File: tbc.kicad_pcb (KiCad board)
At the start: 2 copper layers, 161.3 x 77.6 mm, 51 parts, among them J1 5749181-1, J2 PJRAN1X1U01X, J3 PJRAN1X1U01X, J4 5749181-1, J5 PJRAN1X1U01X, J6 PJRAN3X1U03X, J7 4840.2201, Q1 BSS308PE, SW2 A11AH, U1 SAA7114H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

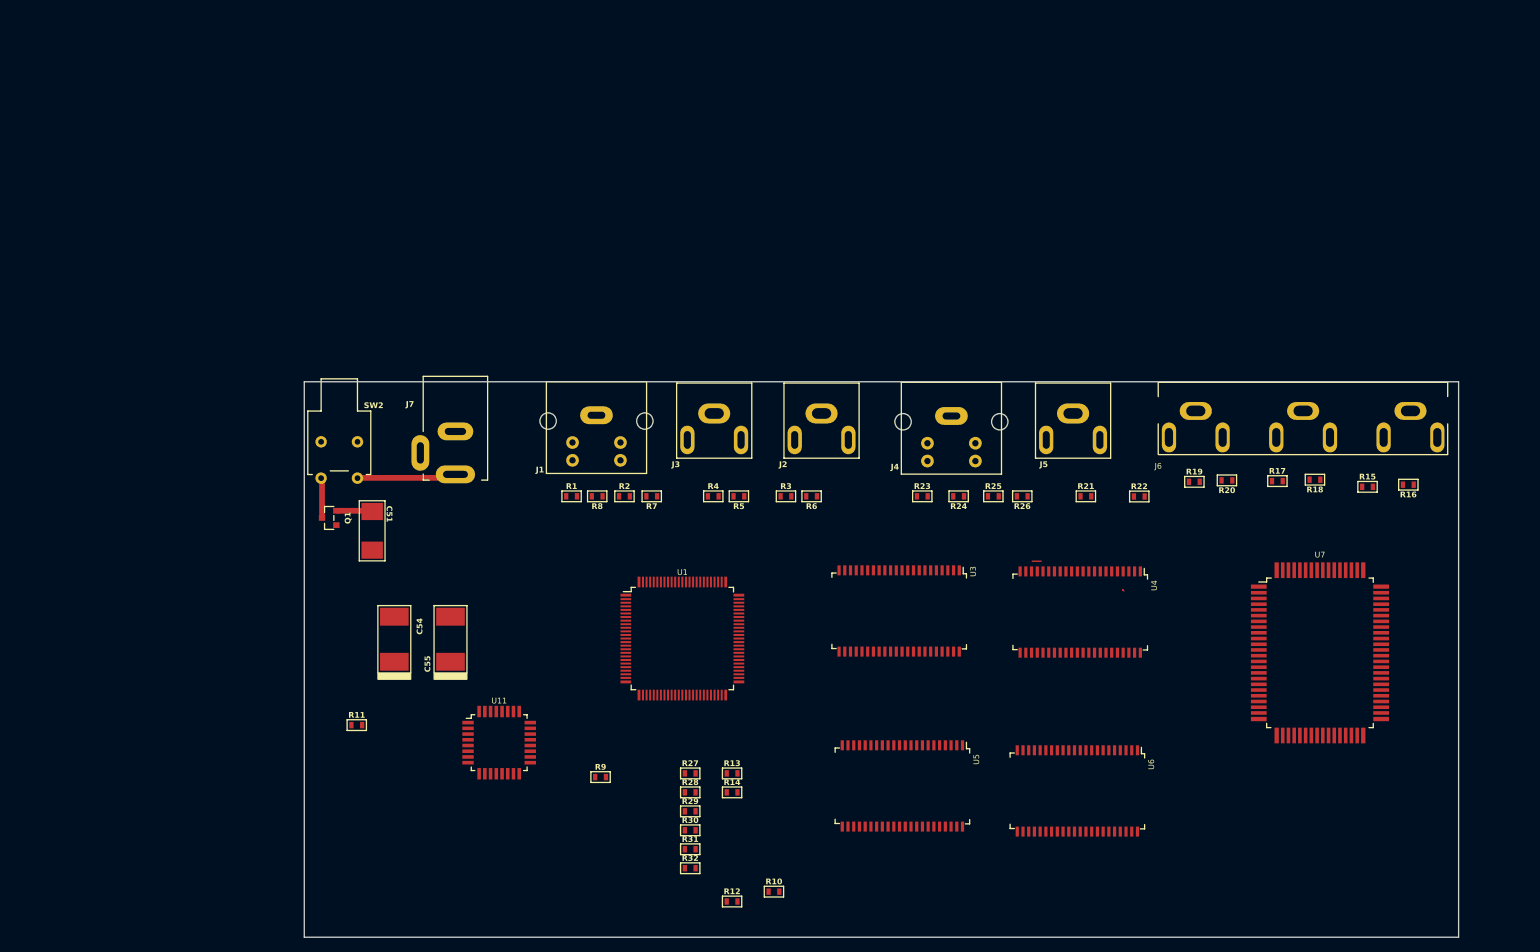
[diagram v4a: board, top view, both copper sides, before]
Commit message: completed power footprints
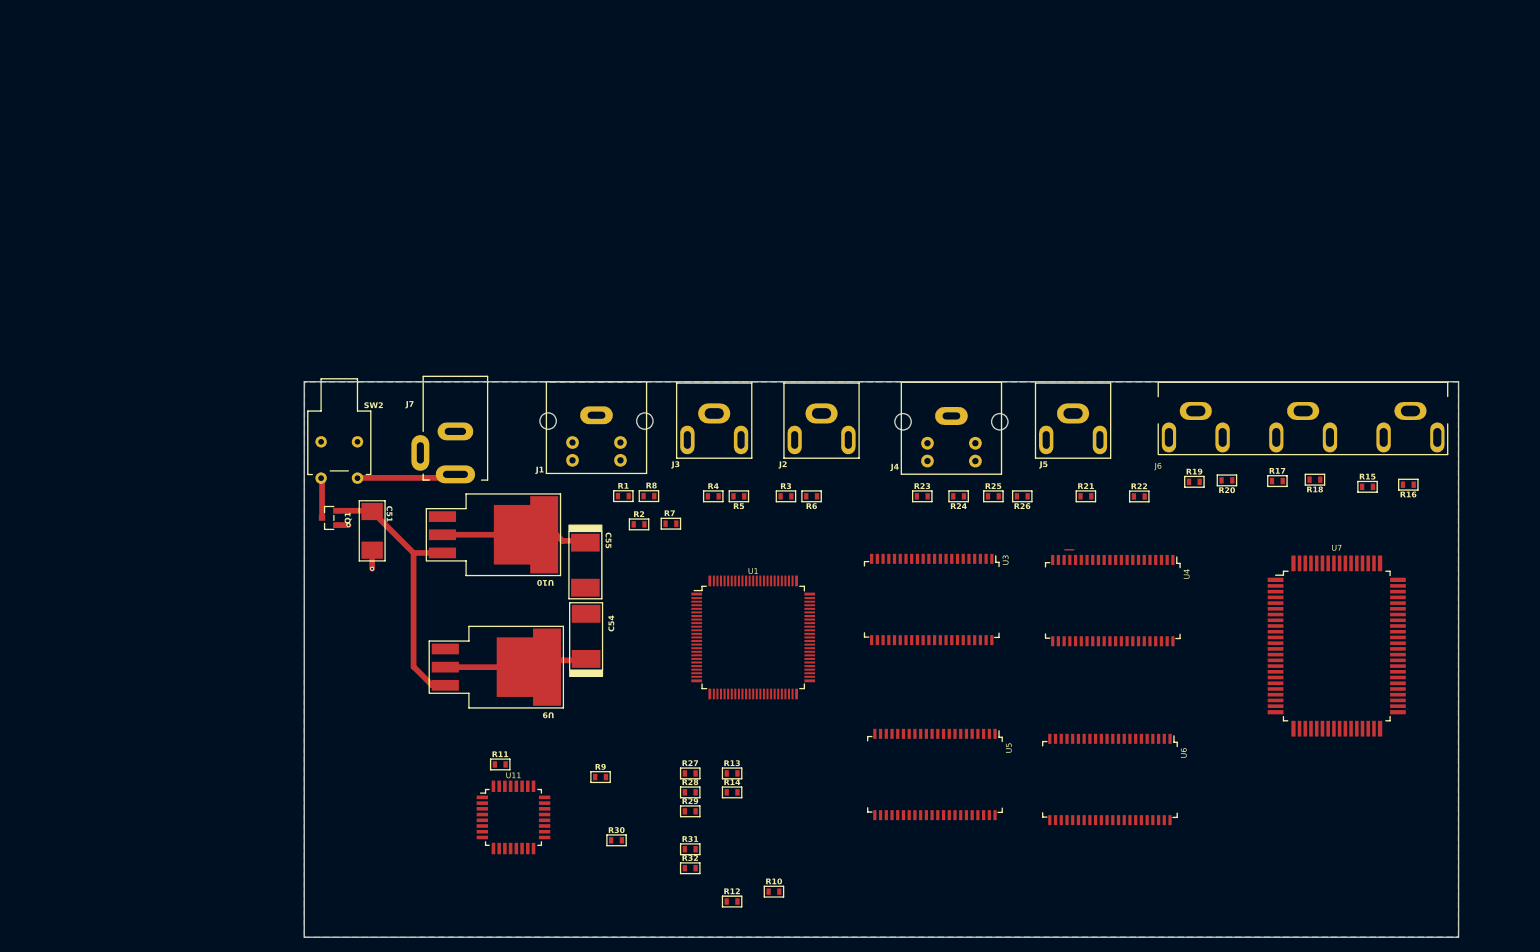
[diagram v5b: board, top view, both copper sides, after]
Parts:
- added U10: LM1086CS-5.0, tbc:TO-263_4.83mm, F.Cu at (108.7, 86.7)
- added U9: LM1086CS-3.3, tbc:TO-263_4.83mm, F.Cu at (109.1, 105.2)
- moved C54 26.8 mm to (128.8, 100.8)
- moved C55 21.5 mm to (128.7, 90.9), turned to -90 degrees
- moved R11 20.8 mm to (116.8, 118.8)
- moved U11 10.6 mm to (118.6, 126.2)
- moved R30 10.4 mm to (133.0, 129.3)
- moved U1 9.90 mm to (152.1, 101.0)
- moved R1 7.23 mm to (133.9, 81.2)
- moved R8 7.23 mm to (137.5, 81.2)
- moved U3 4.82 mm to (177.1, 95.7)
- moved U5 4.82 mm to (177.5, 120.2)
- moved U4 4.82 mm to (202.3, 95.8)
- moved U6 4.82 mm to (201.9, 120.8)
- moved R7 4.67 mm to (140.6, 85.1)
- moved R2 4.42 mm to (136.2, 85.2)
- moved U7 2.53 mm to (233.7, 102.2)
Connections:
- net Net-(Q1-S) renamed /Microcontroller, Power/PIN
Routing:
- net /Microcontroller, Power/PIN: track 4.98 -> 38.6 mm
- net +5V: track 0.00 -> 16.9 mm
- net +3V3: track 0.00 -> 16.6 mm
- net GND: track 0.00 -> 4.30 mm, vias 0 -> 2
- added copper zone on B.Cu, net GND

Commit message: footprints and 3d models for caps, connectors
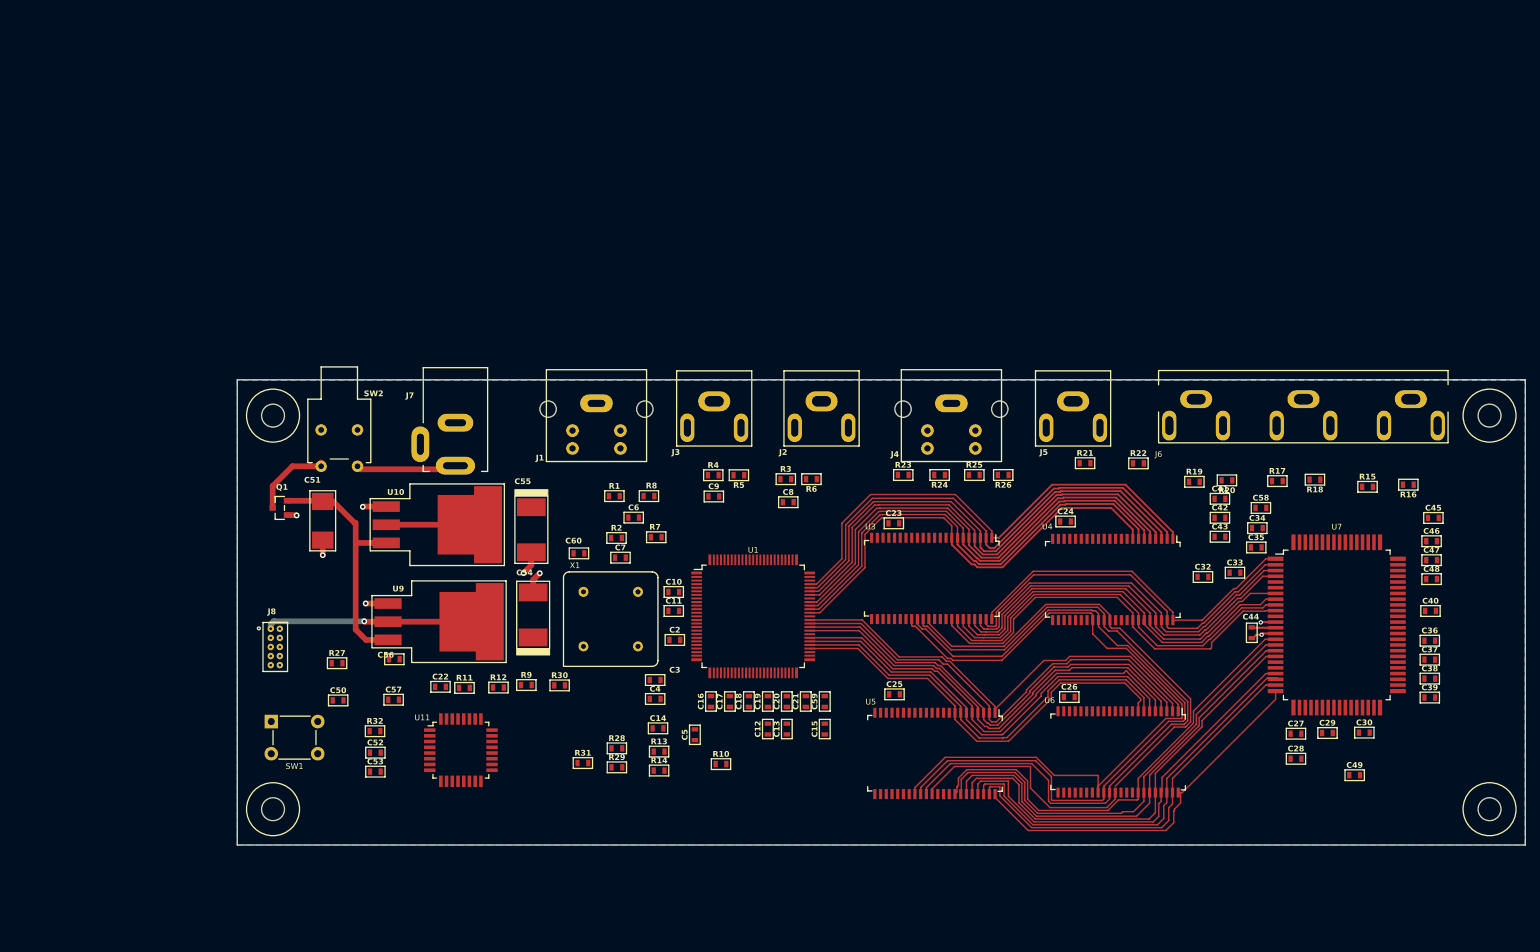
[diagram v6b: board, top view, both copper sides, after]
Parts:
- added C10: 47n, tbc:C0603, F.Cu at (141.0, 94.7)
- added C11: 47n, tbc:C0603, F.Cu at (141.0, 97.3)
- added C12: 100n, tbc:C0603, F.Cu at (154.2, 113.8)
- added C13: 100n, tbc:C0603, F.Cu at (156.8, 113.8)
- added C14: 100n, tbc:C0603, F.Cu at (138.8, 113.7)
- added C15: 100n, tbc:C0603, F.Cu at (162.1, 113.8)
- added C16: 100n, tbc:C0603, F.Cu at (146.2, 110.0)
- added C17: 100n, tbc:C0603, F.Cu at (148.8, 110.0)
- added C18: 100n, tbc:C0603, F.Cu at (151.5, 110.0)
- added C19: 100n, tbc:C0603, F.Cu at (154.2, 110.0)
- added C2: 100n, tbc:C0603, F.Cu at (141.2, 101.3)
- added C20: 100n, tbc:C0603, F.Cu at (156.8, 110.0)
- added C21: 100n, tbc:C0603, F.Cu at (159.4, 110.0)
- added C22: 100n, tbc:C0603, F.Cu at (108.4, 107.9)
- added C23: 100n, tbc:C0603, F.Cu at (171.8, 85.0)
- added C24: 100n, tbc:C0603, F.Cu at (195.8, 84.8)
- added C25: 100n, tbc:C0603, F.Cu at (171.8, 109.0)
- added C26: 100n, tbc:C0603, F.Cu at (196.3, 109.3)
- added C27: 27pF, tbc:C0603, F.Cu at (227.9, 114.5)
- added C28: 27pF, tbc:C0603, F.Cu at (227.9, 118.0)
- added C29: 1n, tbc:C0603, F.Cu at (232.3, 114.3)
- added C3: 100n, tbc:C0603, F.Cu at (138.4, 107.0)
- added C30: 100n, tbc:C0603, F.Cu at (237.5, 114.3)
- added C32: 100n, tbc:C0603, F.Cu at (214.9, 92.5)
- added C33: 100n, tbc:C0603, F.Cu at (219.4, 92.0)
- added C34: 100n, tbc:C0603, F.Cu at (222.6, 85.7)
- added C35: 100n, tbc:C0603, F.Cu at (222.4, 88.4)
- added C36: 100n, tbc:C0603, F.Cu at (246.7, 101.5)
- added C37: 100n, tbc:C0603, F.Cu at (246.7, 104.1)
- added C38: 100n, tbc:C0603, F.Cu at (246.7, 106.8)
- added C39: 100n, tbc:C0603, F.Cu at (246.7, 109.4)
- added C4: 100n, tbc:C0603, F.Cu at (138.4, 109.6)
- added C40: 100n, tbc:C0603, F.Cu at (246.8, 97.3)
- added C41: 100n, tbc:C0603, F.Cu at (217.3, 81.6)
- added C42: 100n, tbc:C0603, F.Cu at (217.3, 84.3)
- added C43: 100n, tbc:C0603, F.Cu at (217.3, 86.9)
- added C44: 100n, tbc:C0603, F.Cu at (221.8, 100.3)
- added C45: 100n, tbc:C0603, F.Cu at (247.2, 84.3)
- added C46: 100n, tbc:C0603, F.Cu at (246.9, 87.5)
- added C47: 100n, tbc:C0603, F.Cu at (246.9, 90.2)
- added C48: 100n, tbc:C0603, F.Cu at (246.9, 92.8)
- added C49: 100n, tbc:C0603, F.Cu at (236.2, 120.2)
- added C5: 100n, tbc:C0603, F.Cu at (143.9, 114.6)
- added C50: 100n, tbc:C0603, F.Cu at (94.1, 109.8)
- added C52: 27pF, tbc:C0603, F.Cu at (99.3, 117.1)
- added C53: 27pF, tbc:C0603, F.Cu at (99.3, 119.8)
- added C56: 4.7u|16V, tbc:C0603, F.Cu at (102.0, 104.0)
- added C57: 100n, tbc:C0603, F.Cu at (101.8, 109.7)
- added C58: 100n, tbc:C0603, F.Cu at (223.1, 82.9)
- added C59: 100n, tbc:C0603, F.Cu at (162.1, 110.0)
- added C6: 47n, tbc:C0603, F.Cu at (135.4, 84.2)
- added C60: 0.01u, tbc:C0603, F.Cu at (127.8, 89.2)
- added C7: 47n, tbc:C0603, F.Cu at (133.6, 89.8)
- added C8: 47n, tbc:C0603, F.Cu at (157.0, 82.1)
- added C9: 47n, tbc:C0603, F.Cu at (146.6, 81.3)
- added J8: 20021111-00010T4LF, tbc:20021111-00010T4LF, F.Cu at (85.3, 102.3)
- added MH1: MH_7.4MMNCx3.2MMD, tbc:MH_7.4MMCx3.2MMD_NON_COPPER_NPTH, F.Cu at (85.0, 70.0)
- added MH2: MH_7.4MMNCx3.2MMD, tbc:MH_7.4MMCx3.2MMD_NON_COPPER_NPTH, F.Cu at (85.0, 125.0)
- added MH3: MH_7.4MMNCx3.2MMD, tbc:MH_7.4MMCx3.2MMD_NON_COPPER_NPTH, F.Cu at (255.0, 70.0)
- added MH4: MH_7.4MMNCx3.2MMD, tbc:MH_7.4MMCx3.2MMD_NON_COPPER_NPTH, F.Cu at (255.0, 125.0)
- added SW1: 1825910-6, tbc:1825910-6, F.Cu at (88.0, 115.0)
- added X1: ACHL-24.576MHZ-EK, tbc:ACHL, F.Cu at (132.2, 98.4)
- moved R27 51.7 mm to (94.0, 104.6)
- moved R32 48.0 mm to (99.2, 114.1)
- moved R12 44.3 mm to (116.5, 108.0)
- moved R30 23.1 mm to (125.0, 107.7)
- moved R10 19.3 mm to (147.6, 118.7)
- moved R31 19.2 mm to (128.3, 118.5)
- moved R9 16.5 mm to (120.4, 107.7)
- moved R28 12.0 mm to (133.1, 116.5)
- moved R29 12.0 mm to (133.1, 119.2)
- moved U11 11.9 mm to (111.2, 116.8)
- moved R11 11.8 mm to (111.8, 108.0)
- moved R14 10.6 mm to (138.9, 119.6)
- moved R13 10.6 mm to (138.9, 117.0)
- moved U9 10.2 mm to (101.1, 98.8)
- moved C55 9.03 mm to (121.1, 86.0)
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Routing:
- net /Frame Memories and Freeze/RCV1: track 0.00 -> 100.7 mm
- net /Frame Memories and Freeze/RCV2: track 0.00 -> 100.6 mm
- net /Frame Memories and Freeze/LLC: track 0.00 -> 99.6 mm
- net /Frame Memories and Freeze/CREF: track 0.00 -> 98.1 mm
- net /Frame Memories and Freeze/HPD1: track 0.00 -> 68.9 mm
- net /Frame Memories and Freeze/HPD2: track 0.00 -> 68.2 mm
- net /Frame Memories and Freeze/HPD0: track 1.25 -> 68.7 mm
- net /Frame Memories and Freeze/HPD3: track 0.00 -> 67.2 mm
- net /Frame Memories and Freeze/HPD4: track 0.00 -> 66.4 mm
- net /Frame Memories and Freeze/HPD5: track 0.00 -> 65.5 mm
- net /Frame Memories and Freeze/IPD1: track 0.00 -> 64.9 mm
- net /Frame Memories and Freeze/HPD6: track 0.00 -> 64.7 mm
- net /Frame Memories and Freeze/IPD0: track 0.00 -> 64.7 mm
- net /Frame Memories and Freeze/HPD7: track 0.00 -> 63.8 mm
- net /Frame Memories and Freeze/MP7: track 0.00 -> 63.7 mm
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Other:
- board size 161.3 x 77.6 mm -> 180 x 65 mm

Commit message: initial work on layout
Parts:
- added C61: 100n, tbc:C0603, F.Cu at (147.3, 122.7)
- added U2: SN74HC00DR, tbc:SOIC-14, F.Cu at (155.7, 122.0)
- added U8: CD74HC74M96, tbc:SOIC-14, F.Cu at (241.0, 115.0)
- C12, C13, C15, C16, C17, C18, C19, C2, C20, C21, C3, C30, C4, C5, C59, C60: moved to B.Cu
- moved R13 113.0 mm to (249.0, 91.4)
- moved C28 37.2 mm to (255.6, 93.0)
- moved C27 33.6 mm to (256.2, 96.4)
- moved R23 33.1 mm to (206.2, 78.7)
- moved C29 29.7 mm to (252.4, 92.5)
- moved R24 28.0 mm to (206.1, 76.9), turned to 0 degrees
- moved C4 27.4 mm to (154.2, 87.3), turned to 90 degrees
- moved C16 26.9 mm to (158.8, 86.2)
- moved C13 24.5 mm to (158.3, 89.3), turned to 0 degrees
- moved C59 24.3 mm to (157.2, 86.2)
- moved R25 24.2 mm to (206.0, 70.6)
- moved C17 23.8 mm to (148.3, 86.2)
- moved C3 23.7 mm to (151.7, 87.3), turned to 90 degrees
- moved C21 22.5 mm to (148.6, 90.2)
- moved C5 21.9 mm to (156.1, 96.4), turned to -90 degrees
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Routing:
- net +3V3: track 32.6 -> 293.7 mm, vias 1 -> 18
- net +5V: track 10.7 -> 243.1 mm, vias 0 -> 15
- net /Frame Memories and Freeze/IGPH: track 0.00 -> 120.6 mm, vias 0 -> 6
- net /Frame Memories and Freeze/IGPV: track 0.00 -> 119.4 mm, vias 0 -> 4
- net /Frame Memories and Freeze/Q2: track 0.00 -> 108.7 mm, vias 0 -> 3
- net /Frame Memories and Freeze/RCV1: track 100.7 -> 198.5 mm
- net /Frame Memories and Freeze/Q1: track 0.00 -> 93.6 mm, vias 0 -> 2
- net GND: track 22.1 -> 111.4 mm, vias 8 -> 54
- net /Frame Memories and Freeze/RCV2: track 100.6 -> 189.2 mm
- net /Frame Memories and Freeze/IDQ: track 0.00 -> 32.3 mm, vias 0 -> 2
- net /Frame Memories and Freeze/ICLK: track 0.00 -> 31.5 mm, vias 0 -> 2
- net /Microcontroller, Power/SCL: track 0.00 -> 31.2 mm, vias 0 -> 2
- net /Microcontroller, Power/SDA: track 0.00 -> 29.2 mm, vias 0 -> 2
- net /Microcontroller, Power/VENC_RST: track 0.00 -> 29.1 mm, vias 0 -> 2
- net Net-(U7-BLUE): track 0.00 -> 26.3 mm
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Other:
- board size 180 x 65 mm -> 180 x 67 mm
